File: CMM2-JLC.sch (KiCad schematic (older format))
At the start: 100 parts, among them J1 Nunchuck, J2 VGA, J3 EXTERNAL I/O, J4 USB_C_Receptacle_USB2.0, J5 Audio, J6 USB A Host, J7 SWD, J8 Micro_SD_Card_Det, J9 Boot select, SW1 Reset, U1 STM32H743IITx, U2 MT48LC16M16A2P, U3 SRV05-4, U4 CP2102N-A01-GQFN28, U5 DS18B20, U6 AMS1117-3.3, U7 TSOP4838, Y1 32.768 kHz, Y2 8 MHz

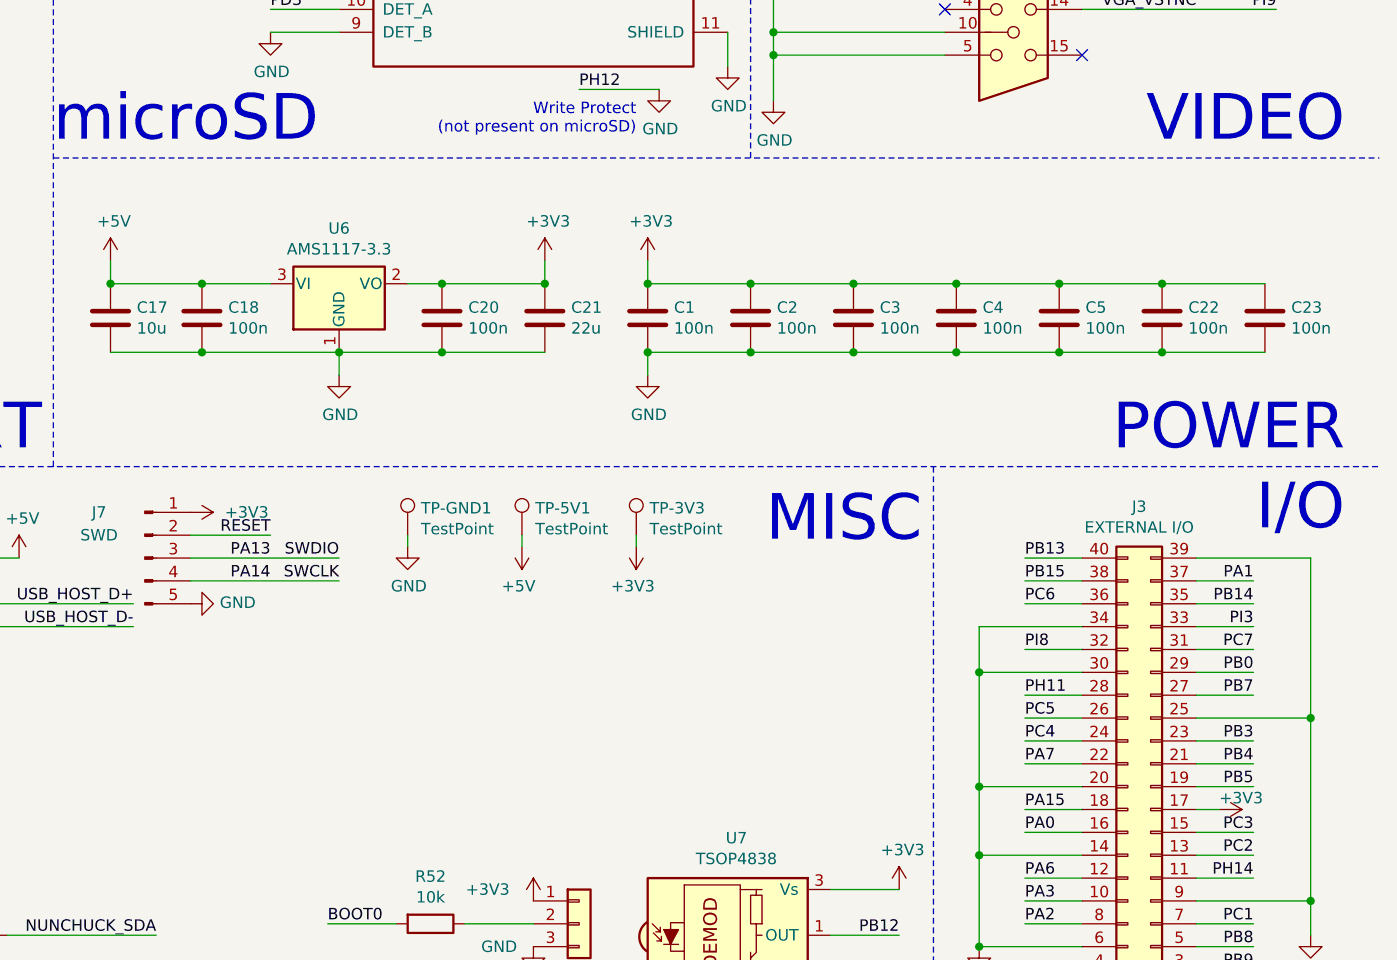
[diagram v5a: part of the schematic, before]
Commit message: Add decoupling, start routing of 40pin extension header
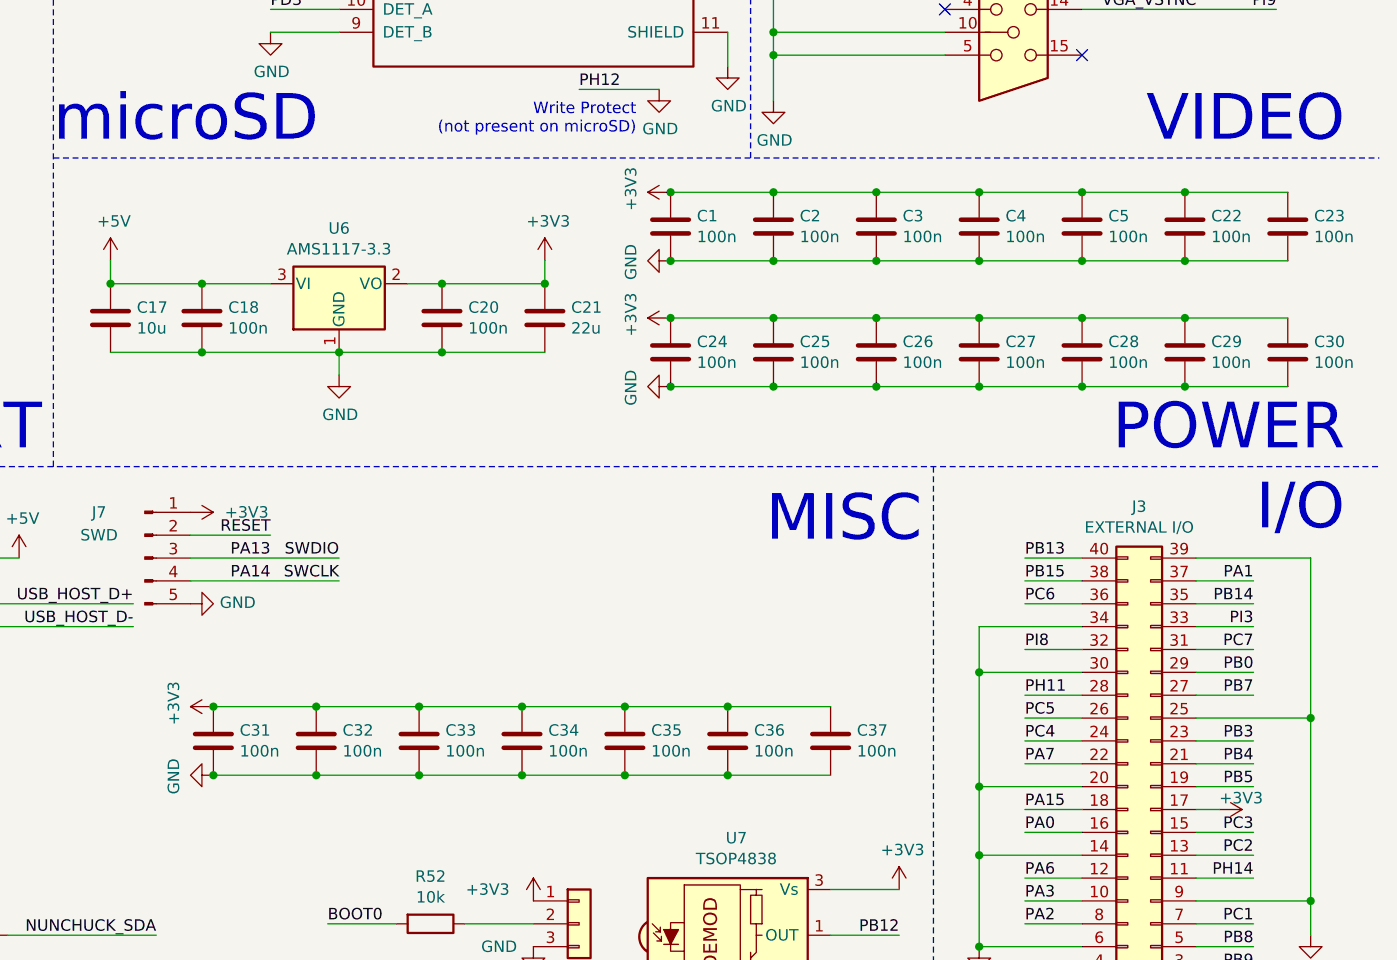
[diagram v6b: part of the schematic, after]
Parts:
- removed TP-3V3, TP-5V1, TP-GND1: TestPoint, TestPoint:TestPoint_Pad_2.0x2.0mm, symbol Connector:TestPoint
- added C24, C25, C26, C27, C28, C29, C30, C31, C32, C33, C34, C35, C36, C37: 100n, Capacitor_SMD:C_0402_1005Metric, symbol Device:C
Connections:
- net +3V3: now also C24.1, C25.1, C26.1, C27.1, C28.1, C29.1, C30.1, C31.1, C32.1, C33.1, C34.1, C35.1, C36.1, C37.1
- net GND: now also C24.2, C25.2, C26.2, C27.2, C28.2, C29.2, C30.2, C31.2, C32.2, C33.2, C34.2, C35.2, C36.2, C37.2
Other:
- moved on the sheet: C1, C2, C22, C23, C3, C4, C5

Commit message: Routed USB, UART and reset pins
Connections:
- net USB_C_D+: now also U3.1 (IO1); no longer U3.3 (IO2)
- net USB_C_D-: now also U3.3 (IO2); no longer U3.1 (IO1)
- net USB_HOST_D+: now also U3.4 (IO3); no longer U3.6 (IO4)
- net USB_HOST_D-: now also U3.6 (IO4); no longer U3.4 (IO3)
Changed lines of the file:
@@
 Text Label 6850 5150 2    50   ~ 0
 USB_C_D-
+Text Label 5400 6800 0    50   ~ 0
+USB_C_D-
 Text Label 5400 6600 0    50   ~ 0
-USB_C_D-
-Text Label 5400 6800 0    50   ~ 0
 USB_C_D+
 Wire Wire Line
@@
 NoConn ~ 6400 5650
 NoConn ~ 6400 5750
+Text Label 7500 6600 2    50   ~ 0
+USB_HOST_D+
 Text Label 7500 6800 2    50   ~ 0
-USB_HOST_D+
-Text Label 7500 6600 2    50   ~ 0
 USB_HOST_D-
 $Comp

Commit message: Fix reversed SDRAM bank select and some style/DRC issues
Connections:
- net PG4: now also U2.20 (BA0); no longer U2.21 (BA1)
- net PG5: now also U2.21 (BA1); no longer U2.20 (BA0)
- net USB_C_D+: now also U3.3 (IO2); no longer U3.1 (IO1)
- net USB_C_D-: now also U3.1 (IO1); no longer U3.3 (IO2)
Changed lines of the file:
@@
 Text Label 5600 9350 0    50   ~ 0
 PG1
+Text Label 5600 9600 0    50   ~ 0
+PG5
 Text Label 5600 9500 0    50   ~ 0
-PG5
-Text Label 5600 9600 0    50   ~ 0
 PG4
 Text Label 5600 9750 0    50   ~ 0
@@
 	5800 9350 5600 9350
 Wire Wire Line
-	5600 9500 5800 9500
-Wire Wire Line
-	5800 9600 5600 9600
+	5600 9600 5800 9600
+Wire Wire Line
+	5800 9500 5600 9500
 Wire Wire Line
 	5600 9750 5800 9750
@@
 Text Label 6850 5150 2    50   ~ 0
 USB_C_D-
+Text Label 5400 6600 0    50   ~ 0
+USB_C_D-
 Text Label 5400 6800 0    50   ~ 0
-USB_C_D-
-Text Label 5400 6600 0    50   ~ 0
 USB_C_D+
 Wire Wire Line
-	5400 6600 5900 6600
-Wire Wire Line
-	5900 6800 5400 6800
+	5400 6800 5900 6800
+Wire Wire Line
+	5900 6600 5400 6600
 Wire Wire Line
 	6400 5150 6850 5150
